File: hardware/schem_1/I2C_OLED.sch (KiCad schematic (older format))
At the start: 9 parts

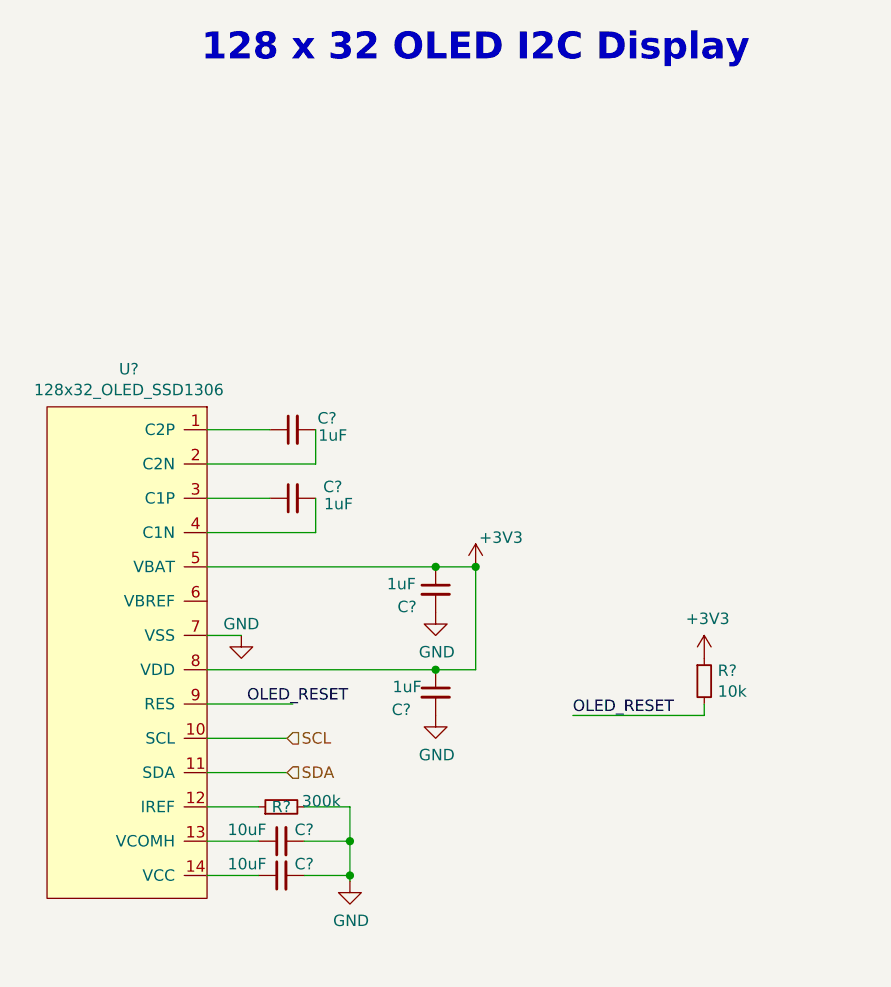
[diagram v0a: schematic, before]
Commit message: update schematic: add io expander with peripherals, update power circuitry- change some components. update project plan. update footprints
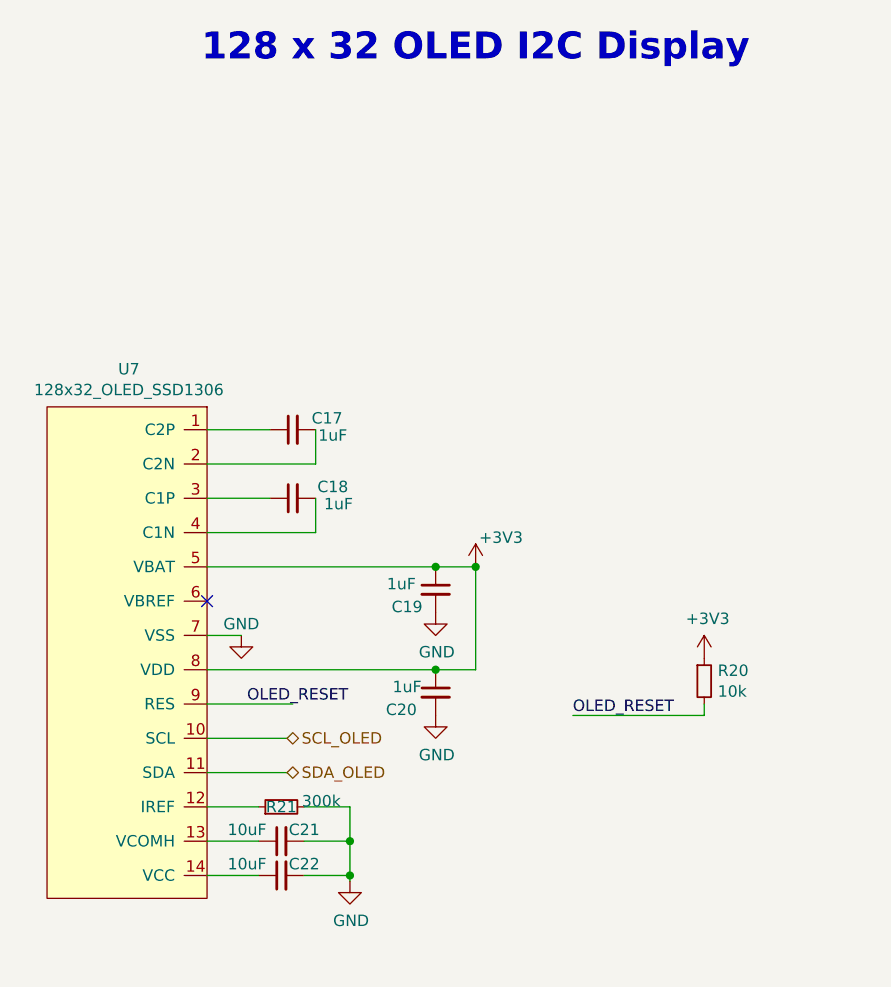
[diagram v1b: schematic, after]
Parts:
- C17, C18, C19, C20: renamed from C?; footprint (none) -> Capacitor_SMD:C_0603_1608Metric
- C21, C22: renamed from C?; footprint (none) -> Capacitor_SMD:C_0805_2012Metric
- U7: renamed from U?; footprint (none) -> Connector_FFC-FPC:TE_1-1734839-4_1x14-1MP_P0.5mm_Horizontal
- gave numbers to parts that had none: 2
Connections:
- net labels added: SCL_OLED, SDA_OLED
- net labels removed: SCL, SDA
- no-connect marks 0 -> 1
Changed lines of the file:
@@
 $Descr A4 11693 8268
 encoding utf-8
-Sheet 3 3
+Sheet 3 4
 Title ""
 Date ""
@@
 $EndDescr
 $Comp
-L Device:C_Small C?
+L Device:C_Small C17
 U 1 1 6176E167
 P 5275 2500
-F 0 "C?" V 5325 2350 50  0000 C CNN
+F 0 "C17" V 5325 2350 50  0000 C CNN
 F 1 "1uF" V 5250 2325 50  0000 C CNN
-F 2 "" H 5275 2500 50  0001 C CNN
+F 2 "Capacitor_SMD:C_0603_1608Metric" H 5275 2500 50  0001 C CNN
 F 3 "~" H 5275 2500 50  0001 C CNN
 	1    5275 2500
@@
 	5375 2650 4900 2650
 $Comp
-L Device:C_Small C?
+L Device:C_Small C18
 U 1 1 6176FB02
 P 5275 2800
-F 0 "C?" V 5325 2625 50  0000 C CNN
+F 0 "C18" V 5325 2625 50  0000 C CNN
 F 1 "1uF" V 5250 2600 50  0000 C CNN
-F 2 "" H 5275 2800 50  0001 C CNN
+F 2 "Capacitor_SMD:C_0603_1608Metric" H 5275 2800 50  0001 C CNN
 F 3 "~" H 5275 2800 50  0001 C CNN
 	1    5275 2800
@@
 	5375 2950 4900 2950
 $Comp
-L power:GND #PWR?
+L power:GND #PWR040
 U 1 1 61776E95
 P 5050 3400
-F 0 "#PWR?" H 5050 3150 50  0001 C CNN
+F 0 "#PWR040" H 5050 3150 50  0001 C CNN
 F 1 "GND" H 5050 3450 50  0000 C CNN
 F 2 "" H 5050 3400 50  0001 C CNN
@@
 	4900 3400 5050 3400
 $Comp
-L power:GND #PWR?
+L power:GND #PWR043
 U 1 1 61777444
 P 5525 4475
-F 0 "#PWR?" H 5525 4225 50  0001 C CNN
+F 0 "#PWR043" H 5525 4225 50  0001 C CNN
 F 1 "GND" H 5530 4302 50  0000 C CNN
 F 2 "" H 5525 4475 50  0001 C CNN
@@
 $EndComp
 $Comp
-L Device:R_Small R?
+L Device:R_Small R21
 U 1 1 617779C2
 P 5225 4150
-F 0 "R?" V 5225 4150 50  0000 C CNN
+F 0 "R21" V 5225 4150 50  0000 C CNN
 F 1 "300k" V 5250 3975 50  0000 C CNN
 F 2 "" H 5225 4150 50  0001 C CNN
@@
 	5525 4150 5525 4300
 $Comp
-L Device:C_Small C?
+L Device:C_Small C21
 U 1 1 617787A9
 P 5225 4300
-F 0 "C?" V 5275 4200 50  0000 C CNN
+F 0 "C21" V 5275 4200 50  0000 C CNN
 F 1 "10uF" V 5275 4450 50  0000 C CNN
-F 2 "" H 5225 4300 50  0001 C CNN
+F 2 "Capacitor_SMD:C_0805_2012Metric" H 5225 4300 50  0001 C CNN
 F 3 "~" H 5225 4300 50  0001 C CNN
 	1    5225 4300
@@
 	5525 4300 5525 4450
 $Comp
-L Device:C_Small C?
+L Device:C_Small C22
 U 1 1 61779F2D
 P 5225 4450
-F 0 "C?" V 5275 4350 50  0000 C CNN
+F 0 "C22" V 5275 4350 50  0000 C CNN
 F 1 "10uF" V 5275 4600 50  0000 C CNN
-F 2 "" H 5225 4450 50  0001 C CNN
+F 2 "Capacitor_SMD:C_0805_2012Metric" H 5225 4450 50  0001 C CNN
 F 3 "~" H 5225 4450 50  0001 C CNN
 	1    5225 4450
@@
 	5525 4450 5525 4475
 $Comp
-L power:GND #PWR?
+L power:GND #PWR042
 U 1 1 6177651C
 P 5900 3750
-F 0 "#PWR?" H 5900 3500 50  0001 C CNN
+F 0 "#PWR042" H 5900 3500 50  0001 C CNN
 F 1 "GND" H 5905 3577 50  0000 C CNN
 F 2 "" H 5900 3750 50  0001 C CNN
@@
 $EndComp
 $Comp
-L Device:C_Small C?
+L Device:C_Small C20
 U 1 1 61774D0A
 P 5900 3650
-F 0 "C?" H 5750 3575 50  0000 C CNN
+F 0 "C20" H 5750 3575 50  0000 C CNN
 F 1 "1uF" H 5775 3675 50  0000 C CNN
-F 2 "" H 5900 3650 50  0001 C CNN
+F 2 "Capacitor_SMD:C_0603_1608Metric" H 5900 3650 50  0001 C CNN
 F 3 "~" H 5900 3650 50  0001 C CNN
 	1    5900 3650
@@
 $EndComp
 $Comp
-L power:+3V3 #PWR?
+L power:+3V3 #PWR038
 U 1 1 61770EE4
 P 6075 3100
-F 0 "#PWR?" H 6075 2950 50  0001 C CNN
+F 0 "#PWR038" H 6075 2950 50  0001 C CNN
 F 1 "+3V3" H 6090 3228 50  0000 L CNN
 F 2 "" H 6075 3100 50  0001 C CNN
@@
 $EndComp
 $Comp
-L power:GND #PWR?
+L power:GND #PWR039
 U 1 1 61780FC5
 P 5900 3300
-F 0 "#PWR?" H 5900 3050 50  0001 C CNN
+F 0 "#PWR039" H 5900 3050 50  0001 C CNN
 F 1 "GND" H 5905 3127 50  0000 C CNN
 F 2 "" H 5900 3300 50  0001 C CNN
@@
 $EndComp
 $Comp
-L Device:C_Small C?
+L Device:C_Small C19
 U 1 1 617810B1
 P 5900 3200
-F 0 "C?" H 5775 3125 50  0000 C CNN
+F 0 "C19" H 5775 3125 50  0000 C CNN
 F 1 "1uF" H 5750 3225 50  0000 C CNN
-F 2 "" H 5900 3200 50  0001 C CNN
+F 2 "Capacitor_SMD:C_0603_1608Metric" H 5900 3200 50  0001 C CNN
 F 3 "~" H 5900 3200 50  0001 C CNN
 	1    5900 3200
@@
 Wire Wire Line
 	4900 4000 5250 4000
-Text HLabel 5250 4000 2    50   Input ~ 0
-SDA
-Text HLabel 5250 3850 2    50   Input ~ 0
-SCL
+Text HLabel 5250 4000 2    50   BiDi ~ 0
+SDA_OLED
+Text HLabel 5250 3850 2    50   BiDi ~ 0
+SCL_OLED
 Wire Wire Line
 	5250 3850 4900 3850
@@
 	6500 3750 7075 3750
 $Comp
-L Device:R_Small R?
+L Device:R_Small R20
 U 1 1 61789AE5
 P 7075 3600
-F 0 "R?" H 7134 3646 50  0000 L CNN
+F 0 "R20" H 7134 3646 50  0000 L CNN
 F 1 "10k" H 7134 3555 50  0000 L CNN
 F 2 "" H 7075 3600 50  0001 C CNN
@@
 $EndComp
 $Comp
-L power:+3V3 #PWR?
+L power:+3V3 #PWR041
 U 1 1 6178A080
 P 7075 3500
-F 0 "#PWR?" H 7075 3350 50  0001 C CNN
+F 0 "#PWR041" H 7075 3350 50  0001 C CNN
 F 1 "+3V3" H 7090 3673 50  0000 C CNN
 F 2 "" H 7075 3500 50  0001 C CNN
@@
 128 x 32 OLED I2C Display
 $Comp
-L library_new_1:128x32_OLED_SSD1306 U?
+L library_new_1:128x32_OLED_SSD1306 U7
 U 1 1 6191EB89
 P 5900 2050
-F 0 "U?" H 4558 1865 50  0000 C CNN
+F 0 "U7" H 4558 1865 50  0000 C CNN
 F 1 "128x32_OLED_SSD1306" H 4558 1774 50  0000 C CNN
-F 2 "" H 5900 2050 50  0001 C CNN
+F 2 "Connector_FFC-FPC:TE_1-1734839-4_1x14-1MP_P0.5mm_Horizontal" H 5900 2050 50  0001 C CNN
 F 3 "" H 5900 2050 50  0001 C CNN
 	1    5900 2050
@@
 	5900 3550 6075 3550
 Connection ~ 6075 3100
+NoConn ~ 4900 3250
 $EndSCHEMATC

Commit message: Replace ESP32 Wroom module with WRover and remove the external PSRAM (as Wrover has one built in). Create symbol and footprint for Wrover. Update footprints for resistors and buttons. Update USB footprint as it was not matching symbol.
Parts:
- R20, R21: footprint (none) -> Resistor_SMD:R_0603_1608Metric
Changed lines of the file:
@@
 F 0 "R21" V 5225 4150 50  0000 C CNN
 F 1 "300k" V 5250 3975 50  0000 C CNN
-F 2 "" H 5225 4150 50  0001 C CNN
+F 2 "Resistor_SMD:R_0603_1608Metric" H 5225 4150 50  0001 C CNN
 F 3 "~" H 5225 4150 50  0001 C CNN
 	1    5225 4150
@@
 F 0 "R20" H 7134 3646 50  0000 L CNN
 F 1 "10k" H 7134 3555 50  0000 L CNN
-F 2 "" H 7075 3600 50  0001 C CNN
+F 2 "Resistor_SMD:R_0603_1608Metric" H 7075 3600 50  0001 C CNN
 F 3 "~" H 7075 3600 50  0001 C CNN
 	1    7075 3600

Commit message: update footprint for OLED display (no longer using ffc connector)
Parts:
- U7: footprint Connector_FFC-FPC:TE_1-1734839-4_1x14-1MP_P0.5mm_Horizontal -> kicad_lib:ER-OLED0.91-7W_SSD1306
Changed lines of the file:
@@
 F 0 "U7" H 4558 1865 50  0000 C CNN
 F 1 "128x32_OLED_SSD1306" H 4558 1774 50  0000 C CNN
-F 2 "Connector_FFC-FPC:TE_1-1734839-4_1x14-1MP_P0.5mm_Horizontal" H 5900 2050 50  0001 C CNN
+F 2 "kicad_lib:ER-OLED0.91-7W_SSD1306" H 5900 2050 50  0001 C CNN
 F 3 "" H 5900 2050 50  0001 C CNN
 	1    5900 2050

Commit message: update footprints for 24way connector, 3D models. add new connector to connect the two PCB's
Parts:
- added R10, R9: 3.3k, Resistor_SMD:R_0603_1608Metric, symbol Device:R_Small
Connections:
- net labels added: +3.3V, SCL, SDA
- wire segments 26 -> 36
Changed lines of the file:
@@
 Wire Wire Line
 	5900 3550 4900 3550
-Wire Wire Line
-	4900 4000 5250 4000
-Text HLabel 5250 4000 2    50   BiDi ~ 0
+Text HLabel 6355 2030 2    50   BiDi ~ 0
 SDA_OLED
-Text HLabel 5250 3850 2    50   BiDi ~ 0
+Text HLabel 6360 1890 2    50   BiDi ~ 0
 SCL_OLED
-Wire Wire Line
-	5250 3850 4900 3850
 Wire Wire Line
 	4900 3700 5275 3700
@@
 Connection ~ 6075 3100
 NoConn ~ 4900 3250
+$Comp
+L Device:R_Small R?
+U 1 1 60D08B52
+P 7055 4375
+AR Path="/60ABC438/60D08B52" Ref="R?"  Part="1"
+AR Path="/61768D59/60D08B52" Ref="R9"  Part="1"
+F 0 "R9" H 6875 4415 50  0000 L CNN
+F 1 "3.3k" H 6845 4325 50  0000 L CNN
+F 2 "Resistor_SMD:R_0603_1608Metric" H 7055 4375 50  0001 C CNN
+F 3 "~" H 7055 4375 50  0001 C CNN
+	1    7055 4375
+	1    0    0    -1
+$EndComp
+$Comp
+L power:+3.3V #PWR?
+U 1 1 60D08B58
+P 7055 4185
+AR Path="/60ABC438/60D08B58" Ref="#PWR?"  Part="1"
+AR Path="/61768D59/60D08B58" Ref="#PWR0101"  Part="1"
+F 0 "#PWR0101" H 7055 4035 50  0001 C CNN
+F 1 "+3.3V" H 7070 4358 50  0000 C CNN
+F 2 "" H 7055 4185 50  0001 C CNN
+F 3 "" H 7055 4185 50  0001 C CNN
+	1    7055 4185
+	1    0    0    -1
+$EndComp
+Wire Wire Line
+	7055 4475 7055 4750
+$Comp
+L Device:R_Small R?
+U 1 1 60D08B5F
+P 7155 4375
+AR Path="/60ABC438/60D08B5F" Ref="R?"  Part="1"
+AR Path="/61768D59/60D08B5F" Ref="R10"  Part="1"
+F 0 "R10" H 7214 4421 50  0000 L CNN
+F 1 "3.3k" H 7214 4330 50  0000 L CNN
+F 2 "Resistor_SMD:R_0603_1608Metric" H 7155 4375 50  0001 C CNN
+F 3 "~" H 7155 4375 50  0001 C CNN
+	1    7155 4375
+	1    0    0    -1
+$EndComp
+Wire Wire Line
+	7155 4475 7155 4850
+Wire Wire Line
+	7055 4185 7055 4225
+Wire Wire Line
+	7155 4275 7155 4225
+Wire Wire Line
+	7155 4225 7055 4225
+Connection ~ 7055 4225
+Wire Wire Line
+	7055 4225 7055 4275
+Text Label 6135 1890 0    50   ~ 0
+SCL
+Wire Wire Line
+	6355 2030 6130 2030
+Text Label 6130 2030 0    50   ~ 0
+SDA
+Wire Wire Line
+	6360 1890 6135 1890
+Text Label 5435 3850 2    50   ~ 0
+SCL
+Text Label 5410 4000 2    50   ~ 0
+SDA
+Wire Wire Line
+	4900 4000 5410 4000
+Wire Wire Line
+	4900 3850 5435 3850
+Text Label 6905 4750 0    50   ~ 0
+SCL
+Text Label 6995 4850 0    50   ~ 0
+SDA
+Wire Wire Line
+	7155 4850 6995 4850
+Wire Wire Line
+	7055 4750 6905 4750
 $EndSCHEMATC

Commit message: update to latest gerbers, update project plan
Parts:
- C17, C18, C19, C20: LCSC (none) -> C15849
- C21, C22: LCSC (none) -> C15850
- R10, R9: LCSC (none) -> C22978
- R20: LCSC (none) -> C25804
- R21: LCSC (none) -> C23024
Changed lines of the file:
@@
 F 2 "Capacitor_SMD:C_0603_1608Metric" H 5275 2500 50  0001 C CNN
 F 3 "~" H 5275 2500 50  0001 C CNN
+F 4 "C15849" V 5275 2500 50  0001 C CNN "LCSC"
 	1    5275 2500
 	0    -1   -1   0
@@
 F 2 "Capacitor_SMD:C_0603_1608Metric" H 5275 2800 50  0001 C CNN
 F 3 "~" H 5275 2800 50  0001 C CNN
+F 4 "C15849" V 5275 2800 50  0001 C CNN "LCSC"
 	1    5275 2800
 	0    -1   -1   0
@@
 U 1 1 617779C2
 P 5225 4150
-F 0 "R21" V 5225 4150 50  0000 C CNN
+F 0 "R21" V 5295 4155 50  0000 C CNN
 F 1 "300k" V 5250 3975 50  0000 C CNN
 F 2 "Resistor_SMD:R_0603_1608Metric" H 5225 4150 50  0001 C CNN
 F 3 "~" H 5225 4150 50  0001 C CNN
+F 4 "C23024" V 5225 4150 50  0001 C CNN "LCSC"
 	1    5225 4150
 	0    -1   -1   0
@@
 F 2 "Capacitor_SMD:C_0805_2012Metric" H 5225 4300 50  0001 C CNN
 F 3 "~" H 5225 4300 50  0001 C CNN
+F 4 "C15850" V 5225 4300 50  0001 C CNN "LCSC"
 	1    5225 4300
 	0    -1   -1   0
@@
 F 2 "Capacitor_SMD:C_0805_2012Metric" H 5225 4450 50  0001 C CNN
 F 3 "~" H 5225 4450 50  0001 C CNN
+F 4 "C15850" V 5225 4450 50  0001 C CNN "LCSC"
 	1    5225 4450
 	0    -1   -1   0
@@
 F 2 "Capacitor_SMD:C_0603_1608Metric" H 5900 3650 50  0001 C CNN
 F 3 "~" H 5900 3650 50  0001 C CNN
+F 4 "C15849" H 5900 3650 50  0001 C CNN "LCSC"
 	1    5900 3650
 	1    0    0    -1
@@
 F 2 "Capacitor_SMD:C_0603_1608Metric" H 5900 3200 50  0001 C CNN
 F 3 "~" H 5900 3200 50  0001 C CNN
+F 4 "C15849" H 5900 3200 50  0001 C CNN "LCSC"
 	1    5900 3200
 	1    0    0    -1
@@
 F 2 "Resistor_SMD:R_0603_1608Metric" H 7075 3600 50  0001 C CNN
 F 3 "~" H 7075 3600 50  0001 C CNN
+F 4 "C25804" H 7075 3600 50  0001 C CNN "LCSC"
 	1    7075 3600
 	1    0    0    -1
@@
 F 2 "Resistor_SMD:R_0603_1608Metric" H 7055 4375 50  0001 C CNN
 F 3 "~" H 7055 4375 50  0001 C CNN
+F 4 "C22978" H 7055 4375 50  0001 C CNN "LCSC"
 	1    7055 4375
 	1    0    0    -1
@@
 F 2 "Resistor_SMD:R_0603_1608Metric" H 7155 4375 50  0001 C CNN
 F 3 "~" H 7155 4375 50  0001 C CNN
+F 4 "C22978" H 7155 4375 50  0001 C CNN "LCSC"
 	1    7155 4375
 	1    0    0    -1
